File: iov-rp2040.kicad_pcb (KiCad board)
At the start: 2 copper layers, 60 x 60 mm, 43 parts, among them J1 USB_C_Receptacle_USB2.0, J2 SWD, J3 output header, Q1 BC847, SW1 CL-SB-13B-01T, SW2 BSL, SW3 RST, U1 TLV75518PDBV, U2 TLV75533PDBV, U3 AT25FF081A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

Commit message: revision b:
fixed flash footprint
changed ground pour to be cleaner
added name and revision text
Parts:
- U3: footprint Package_SO:SOIC-8_3.9x4.9mm_P1.27mm -> Package_SO:SOIC-8_5.275x5.275mm_P1.27mm
- moved U3 1.25 mm to (153.8, 110.5)
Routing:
- net IOVDD: track 144.0 -> 146.8 mm
- net /QSPI_IO0: track 10.9 -> 13.3 mm
- net /QSPI_SCLK: track 13.9 -> 15.5 mm
- net /QSPI_IO3: track 16.2 -> 17.7 mm
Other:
- board text added: "iov-rp2040 rev: b"

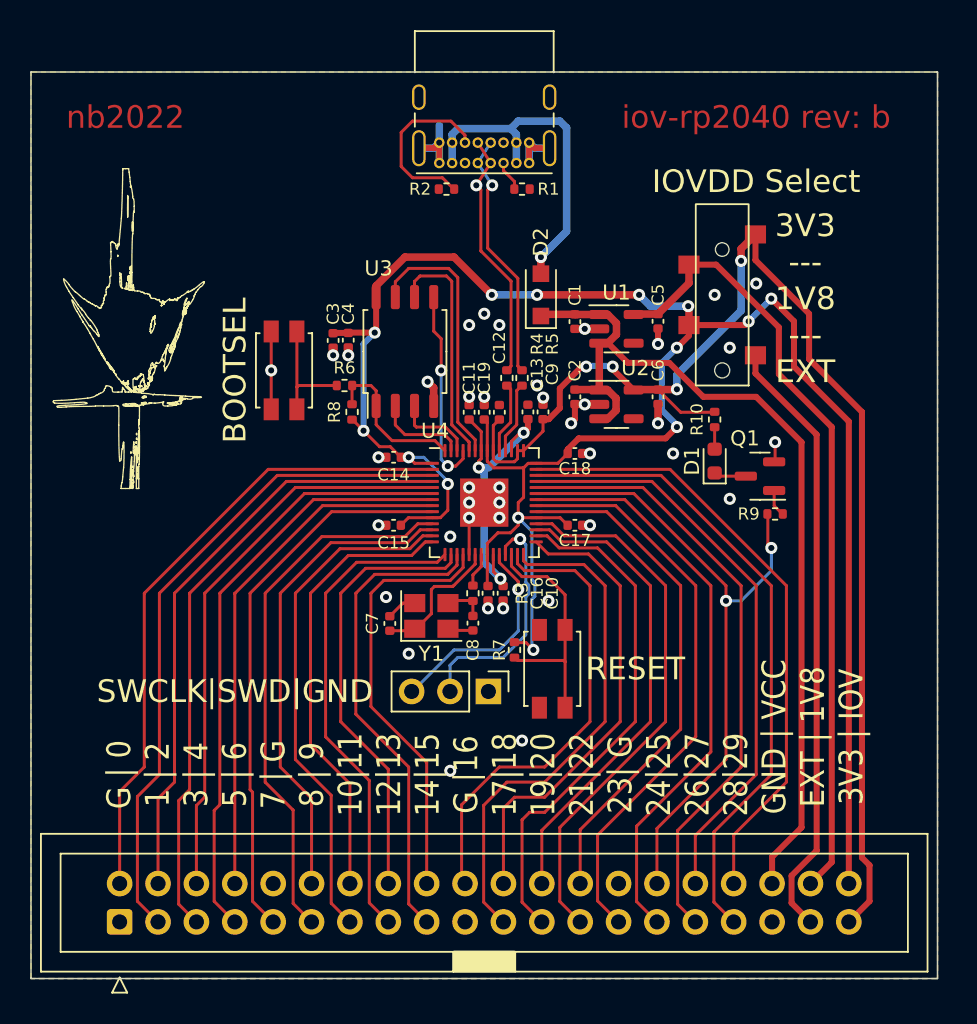
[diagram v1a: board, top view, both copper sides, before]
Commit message: length matched qspi and redid power section
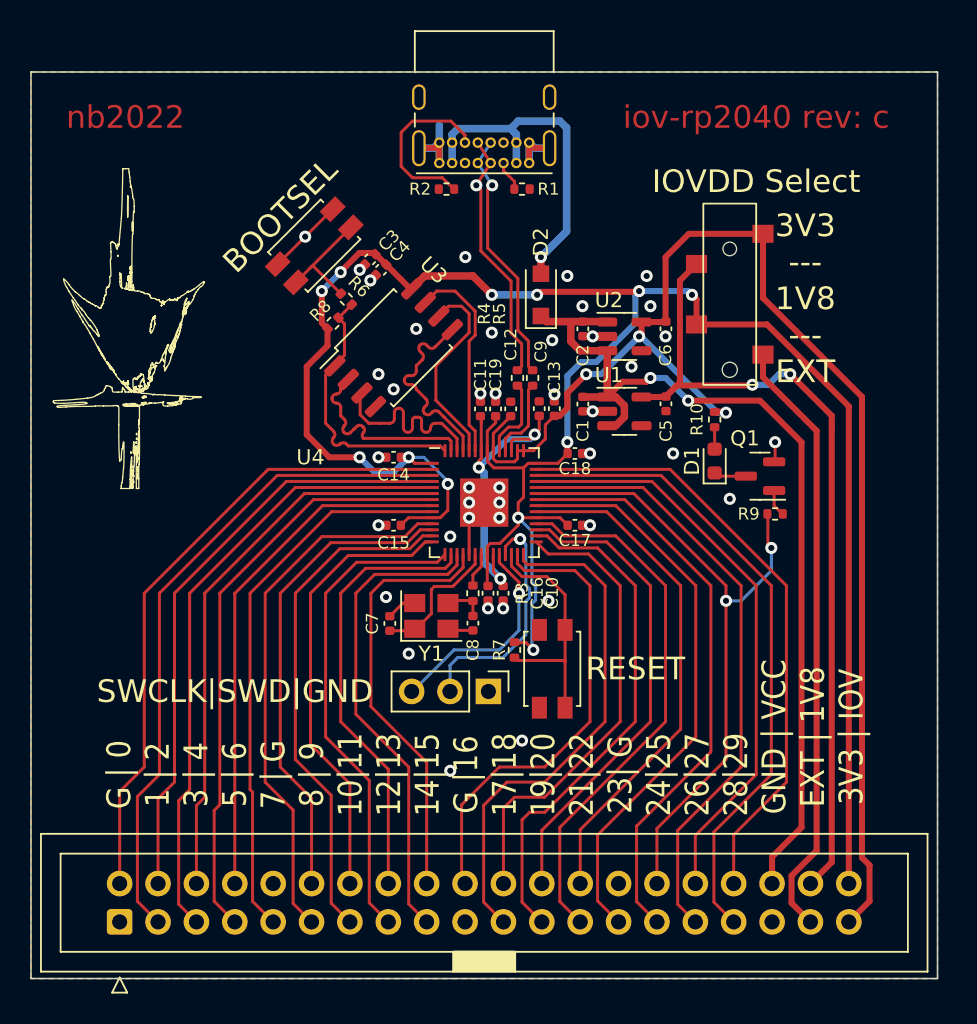
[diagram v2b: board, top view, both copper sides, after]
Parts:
- moved SW2 8.49 mm to (147.8, 103.5), turned to 45 degrees
- moved R8 6.01 mm to (149.0, 108.6), turned to 45 degrees
- moved C3 5.90 mm to (151.4, 104.4), turned to -135 degrees
- moved R6 5.72 mm to (149.9, 107.0), turned to -45 degrees
- moved C1 5.49 mm to (165.5, 114.0)
- moved C5 5.49 mm to (171.0, 114.0)
- moved U1 5.49 mm to (168.3, 114.5)
- moved C4 5.14 mm to (152.2, 105.1), turned to -135 degrees
- moved C2 4.53 mm to (165.5, 109.0)
- moved C6 4.53 mm to (171.0, 109.0)
- moved U2 4.53 mm to (168.3, 109.5)
- moved U3 0.79 mm to (153.0, 110.2), turned to 45 degrees
- moved C11 0.78 mm to (158.8, 114.3)
- moved C12 0.78 mm to (160.8, 114.3)
- moved C13 0.78 mm to (163.6, 114.3)
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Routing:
- net /QSPI_IO2: track 5.26 -> 13.2 mm
- net /QSPI_CS: track 10.6 -> 18.2 mm
- net /QSPI_IO1: track 6.02 -> 13.4 mm
- net GND: track 38.0 -> 32.6 mm, vias 40 -> 41
- net /QSPI_IO3: track 17.7 -> 13.7 mm
- net +3V3: track 85.9 -> 89.8 mm, vias 4 -> 3
- net +1V8: track 52.3 -> 55.5 mm, vias 0 -> 2
- net /QSPI_SCLK: track 15.5 -> 13.4 mm
- net +1V1: track 20.5 -> 22.1 mm
- net IOVDD: track 146.8 -> 148.4 mm, vias 14 -> 12
- net VCC: track 61.7 -> 62.6 mm, vias 0 -> 2
- net /U_P: track 4.75 -> 5.43 mm
- net /U_N: track 4.79 -> 5.45 mm
- net /QSPI_IO0: vias 2 -> 0
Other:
- board text added: "iov-rp2040 rev: c"
- board text removed: "iov-rp2040 rev: b"
